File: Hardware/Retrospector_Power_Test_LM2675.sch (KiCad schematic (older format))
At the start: 21 parts, among them J2 Eurorack_10_pin_power, U1 TPS5410D, U2 LD1117-3.3-4Tab

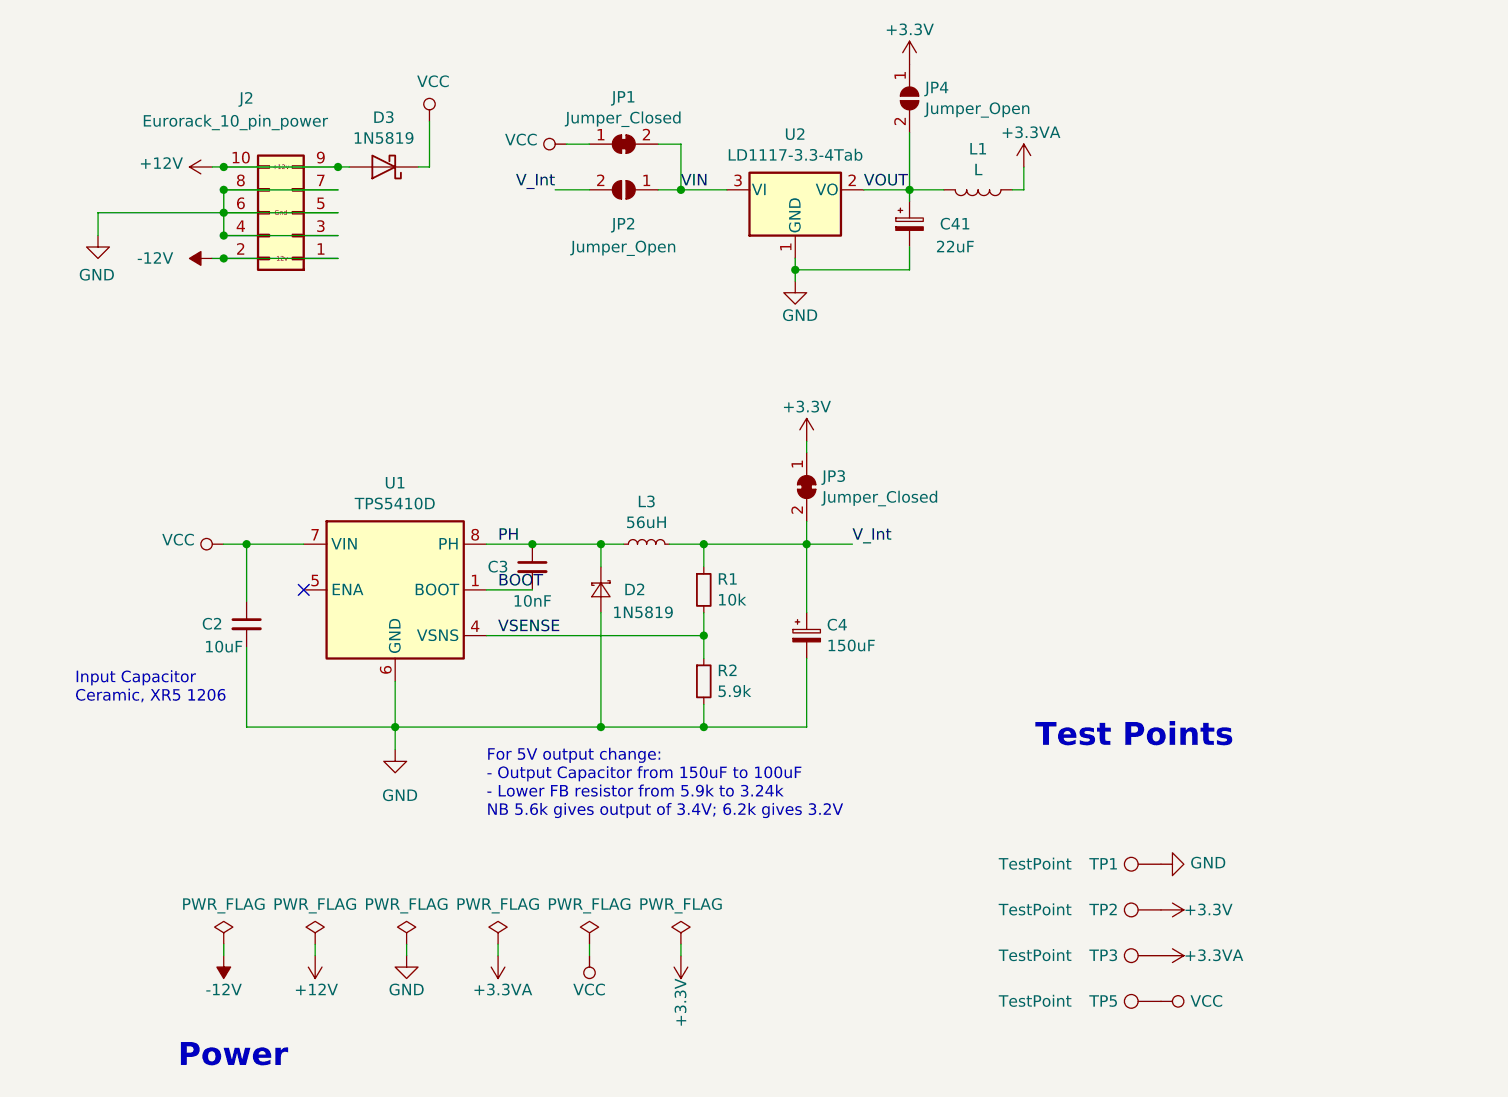
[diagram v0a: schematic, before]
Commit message: Initial schematics for power test boards with various chips
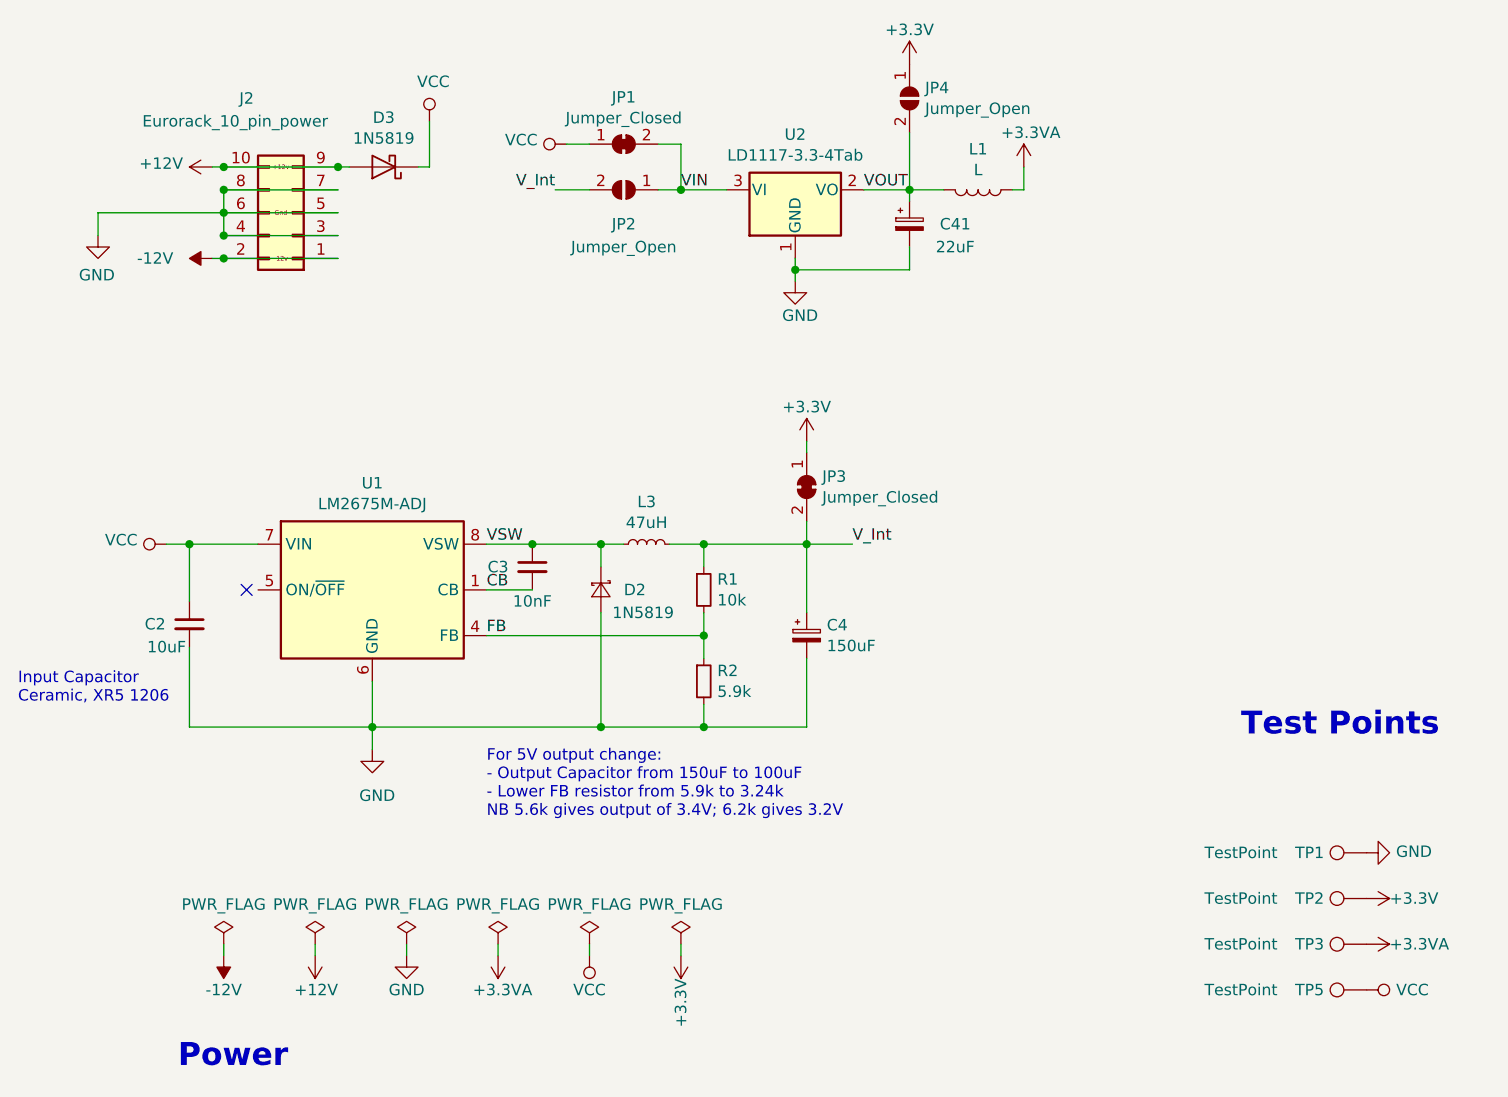
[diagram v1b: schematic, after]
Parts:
- removed U1: TPS5410D, Housings_SOIC:SOIC-8_3.9x4.9mm_Pitch1.27mm, symbol TPS5410DR:TPS5410D
- added U1: LM2675M-ADJ, Housings_SOIC:SOIC-8_3.9x4.9mm_Pitch1.27mm, symbol LM2675M-ADJ:LM2675M-ADJ
- L3: value 56uH -> 47uH; footprint Custom_Footprints:Inductor_SMD_6x6mm -> Inductors_SMD:L_6.3x6.3_H3
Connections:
- net GND: now also U1.6 (GND)
- net VCC: now also U1.7 (VIN)
- net BOOT renamed CB
- net CB: now also U1.1 (CB)
- net PH renamed VSW
- net VSW: now also U1.8 (VSW)
- net VSENSE renamed FB
- net FB: now also U1.4 (FB)
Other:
- moved on the sheet: C2, TP1, TP2, TP3, TP5
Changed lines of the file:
@@
 L Connector:TestPoint TP5
 U 1 1 5FBC912F
-P 5550 4950
-F 0 "TP5" V 5550 5200 50  0000 C CNN
-F 1 "TestPoint" V 5550 5500 50  0000 C CNN
-F 2 "Custom_Footprints:1.3mm_Test_Point" H 5750 4950 50  0001 C CNN
-F 3 "~" H 5750 4950 50  0001 C CNN
-	1    5550 4950
+P 6450 4900
+F 0 "TP5" V 6450 5150 50  0000 C CNN
+F 1 "TestPoint" V 6450 5450 50  0000 C CNN
+F 2 "Custom_Footprints:1.3mm_Test_Point" H 6650 4900 50  0001 C CNN
+F 3 "~" H 6650 4900 50  0001 C CNN
+	1    6450 4900
 	0    -1   -1   0
 $EndComp
@@
 L power:VCC #PWR018
 U 1 1 5FBC9909
-P 5550 4950
-F 0 "#PWR018" H 5550 4800 50  0001 C CNN
-F 1 "VCC" V 5550 5150 50  0000 C CNN
-F 2 "" H 5550 4950 50  0001 C CNN
-F 3 "" H 5550 4950 50  0001 C CNN
-	1    5550 4950
-	0    1    1    0
-$EndComp
-Text Notes 5000 3850 0    100  ~ 20
+P 6450 4900
+F 0 "#PWR018" H 6450 4750 50  0001 C CNN
+F 1 "VCC" V 6450 5100 50  0000 C CNN
+F 2 "" H 6450 4900 50  0001 C CNN
+F 3 "" H 6450 4900 50  0001 C CNN
+	1    6450 4900
+	0    1    1    0
+$EndComp
+Text Notes 5900 3800 0    100  ~ 20
 Test Points
 Wire Wire Line
@@
 L power:+3.3VA #PWR013
 U 1 1 5FBC8BDD
-P 5550 4750
-F 0 "#PWR013" H 5550 4600 50  0001 C CNN
-F 1 "+3.3VA" V 5550 4850 50  0000 L CNN
-F 2 "" H 5550 4750 50  0001 C CNN
-F 3 "" H 5550 4750 50  0001 C CNN
-	1    5550 4750
+P 6450 4700
+F 0 "#PWR013" H 6450 4550 50  0001 C CNN
+F 1 "+3.3VA" V 6450 4800 50  0000 L CNN
+F 2 "" H 6450 4700 50  0001 C CNN
+F 3 "" H 6450 4700 50  0001 C CNN
+	1    6450 4700
 	0    1    1    0
 $EndComp
@@
 L Connector:TestPoint TP3
 U 1 1 5FBC8AAF
-P 5550 4750
-F 0 "TP3" V 5550 5000 50  0000 C CNN
-F 1 "TestPoint" V 5550 5300 50  0000 C CNN
-F 2 "Custom_Footprints:1.3mm_Test_Point" H 5750 4750 50  0001 C CNN
-F 3 "~" H 5750 4750 50  0001 C CNN
-	1    5550 4750
+P 6450 4700
+F 0 "TP3" V 6450 4950 50  0000 C CNN
+F 1 "TestPoint" V 6450 5250 50  0000 C CNN
+F 2 "Custom_Footprints:1.3mm_Test_Point" H 6650 4700 50  0001 C CNN
+F 3 "~" H 6650 4700 50  0001 C CNN
+	1    6450 4700
 	0    -1   -1   0
 $EndComp
@@
 L power:+3.3V #PWR011
 U 1 1 5FBC8425
-P 5550 4550
-F 0 "#PWR011" H 5550 4400 50  0001 C CNN
-F 1 "+3.3V" V 5550 4650 50  0000 L CNN
-F 2 "" H 5550 4550 50  0001 C CNN
-F 3 "" H 5550 4550 50  0001 C CNN
-	1    5550 4550
+P 6450 4500
+F 0 "#PWR011" H 6450 4350 50  0001 C CNN
+F 1 "+3.3V" V 6450 4600 50  0000 L CNN
+F 2 "" H 6450 4500 50  0001 C CNN
+F 3 "" H 6450 4500 50  0001 C CNN
+	1    6450 4500
 	0    1    1    0
 $EndComp
@@
 L Connector:TestPoint TP2
 U 1 1 5FBC80EE
-P 5550 4550
-F 0 "TP2" V 5550 4800 50  0000 C CNN
-F 1 "TestPoint" V 5550 5100 50  0000 C CNN
-F 2 "Custom_Footprints:1.3mm_Test_Point" H 5750 4550 50  0001 C CNN
-F 3 "~" H 5750 4550 50  0001 C CNN
-	1    5550 4550
+P 6450 4500
+F 0 "TP2" V 6450 4750 50  0000 C CNN
+F 1 "TestPoint" V 6450 5050 50  0000 C CNN
+F 2 "Custom_Footprints:1.3mm_Test_Point" H 6650 4500 50  0001 C CNN
+F 3 "~" H 6650 4500 50  0001 C CNN
+	1    6450 4500
 	0    -1   -1   0
 $EndComp
@@
 L power:GND #PWR010
 U 1 1 5FBC7DF8
-P 5550 4350
-F 0 "#PWR010" H 5550 4100 50  0001 C CNN
-F 1 "GND" V 5555 4222 50  0000 R CNN
-F 2 "" H 5550 4350 50  0001 C CNN
-F 3 "" H 5550 4350 50  0001 C CNN
-	1    5550 4350
+P 6450 4300
+F 0 "#PWR010" H 6450 4050 50  0001 C CNN
+F 1 "GND" V 6455 4172 50  0000 R CNN
+F 2 "" H 6450 4300 50  0001 C CNN
+F 3 "" H 6450 4300 50  0001 C CNN
+	1    6450 4300
 	0    -1   -1   0
 $EndComp
@@
 L Connector:TestPoint TP1
 U 1 1 5FBC76F3
-P 5550 4350
-F 0 "TP1" V 5550 4600 50  0000 C CNN
-F 1 "TestPoint" V 5550 4900 50  0000 C CNN
-F 2 "Custom_Footprints:1.3mm_Test_Point" H 5750 4350 50  0001 C CNN
-F 3 "~" H 5750 4350 50  0001 C CNN
-	1    5550 4350
+P 6450 4300
+F 0 "TP1" V 6450 4550 50  0000 C CNN
+F 1 "TestPoint" V 6450 4850 50  0000 C CNN
+F 2 "Custom_Footprints:1.3mm_Test_Point" H 6650 4300 50  0001 C CNN
+F 3 "~" H 6650 4300 50  0001 C CNN
+	1    6450 4300
 	0    -1   -1   0
 $EndComp
 Wire Wire Line
 	1450 1500 900  1500
-$Comp
-L TPS5410DR:TPS5410D U1
-U 1 1 63B9AA59
-P 2200 3150
-F 0 "U1" H 2200 3617 50  0000 C CNN
-F 1 "TPS5410D" H 2200 3526 50  0000 C CNN
-F 2 "Housings_SOIC:SOIC-8_3.9x4.9mm_Pitch1.27mm" H 2150 3600 50  0001 C CNN
-F 3 "https://www.ti.com/lit/gpn/tps5410" H 2200 3150 50  0001 C CNN
-	1    2200 3150
-	1    0    0    -1
-$EndComp
 $Comp
 L Device:C_Small C3
@@
 Wire Wire Line
 	2600 3150 2800 3150
-NoConn ~ 1800 3150
+NoConn ~ 1550 3150
 $Comp
 L power:GND #PWR03
 U 1 1 63BB87EE
-P 2200 3850
-F 0 "#PWR03" H 2200 3600 50  0001 C CNN
-F 1 "GND" H 2300 3650 50  0000 R CNN
-F 2 "" H 2200 3850 50  0001 C CNN
-F 3 "" H 2200 3850 50  0001 C CNN
-	1    2200 3850
-	1    0    0    -1
-$EndComp
-Wire Wire Line
-	2200 3550 2200 3750
-Wire Wire Line
-	1800 2950 1550 2950
-Wire Wire Line
-	1550 2950 1550 3200
-Wire Wire Line
-	1550 3400 1550 3750
-Wire Wire Line
-	1550 3750 2200 3750
-Connection ~ 2200 3750
+P 2100 3850
+F 0 "#PWR03" H 2100 3600 50  0001 C CNN
+F 1 "GND" H 2200 3650 50  0000 R CNN
+F 2 "" H 2100 3850 50  0001 C CNN
+F 3 "" H 2100 3850 50  0001 C CNN
+	1    2100 3850
+	1    0    0    -1
+$EndComp
+Wire Wire Line
+	2100 3550 2100 3750
+Wire Wire Line
+	1600 2950 1300 2950
+Wire Wire Line
+	1300 2950 1300 3200
+Wire Wire Line
+	1300 3400 1300 3750
+Wire Wire Line
+	1300 3750 2100 3750
+Connection ~ 2100 3750
 $Comp
 L power:VCC #PWR01
 U 1 1 63BCE4C9
-P 1450 2950
-F 0 "#PWR01" H 1450 2800 50  0001 C CNN
-F 1 "VCC" V 1468 3077 50  0000 L CNN
-F 2 "" H 1450 2950 50  0001 C CNN
-F 3 "" H 1450 2950 50  0001 C CNN
-	1    1450 2950
-	0    -1   -1   0
-$EndComp
-Wire Wire Line
-	1450 2950 1550 2950
-Connection ~ 1550 2950
-Wire Wire Line
-	2200 3850 2200 3750
+P 1200 2950
+F 0 "#PWR01" H 1200 2800 50  0001 C CNN
+F 1 "VCC" V 1218 3077 50  0000 L CNN
+F 2 "" H 1200 2950 50  0001 C CNN
+F 3 "" H 1200 2950 50  0001 C CNN
+	1    1200 2950
+	0    -1   -1   0
+$EndComp
+Wire Wire Line
+	1200 2950 1300 2950
+Connection ~ 1300 2950
+Wire Wire Line
+	2100 3850 2100 3750
 Connection ~ 3550 3750
 Wire Wire Line
@@
 P 3300 2950
 F 0 "L3" V 3485 2950 50  0000 C CNN
-F 1 "56uH" V 3394 2950 50  0000 C CNN
-F 2 "Custom_Footprints:Inductor_SMD_6x6mm" H 3300 2950 50  0001 C CNN
-F 3 "https://datasheet.lcsc.com/szlcsc/1912111437_3L-COILS-SNR6045K-680M_C326343.pdf" H 3300 2950 50  0001 C CNN
+F 1 "47uH" V 3394 2950 50  0000 C CNN
+F 2 "Inductors_SMD:L_6.3x6.3_H3" H 3300 2950 50  0001 C CNN
+F 3 "https://www.mouser.com/datasheet/2/400/nductor_automotive_power_clf7045-d_en-1280129.pdf" H 3300 2950 50  0001 C CNN
 F 4 "C326343" V 3300 2950 50  0001 C CNN "Part_Number"
 	1    3300 2950
@@
 	3100 3250 3100 3750
 Wire Wire Line
-	3100 3750 2200 3750
-Connection ~ 3100 3750
+	3100 3750 2100 3750
 $Comp
 L power:+3.3V #PWR04
@@
 Text Notes 2600 4150 0    50   ~ 0
 For 5V output change:\n- Output Capacitor from 150uF to 100uF\n- Lower FB resistor from 5.9k to 3.24k\nNB 5.6k gives output of 3.4V; 6.2k gives 3.2V
-Text Notes 800  3650 0    50   ~ 0
+Text Notes 550  3650 0    50   ~ 0
 Input Capacitor\nCeramic, XR5 1206
 $Comp
 L Device:C_Small C2
 U 1 1 63C237DB
-P 1550 3300
-F 0 "C2" H 1400 3300 50  0000 C CNN
-F 1 "10uF" H 1450 3200 50  0000 C CNN
-F 2 "Capacitors_SMD:C_1206" H 1550 3300 50  0001 C CNN
-F 3 "~" H 1550 3300 50  0001 C CNN
-F 4 "C57112" H 1550 3300 50  0001 C CNN "Part_Number"
-	1    1550 3300
+P 1300 3300
+F 0 "C2" H 1150 3300 50  0000 C CNN
+F 1 "10uF" H 1200 3200 50  0000 C CNN
+F 2 "Capacitors_SMD:C_1206" H 1300 3300 50  0001 C CNN
+F 3 "~" H 1300 3300 50  0001 C CNN
+F 4 "C57112" H 1300 3300 50  0001 C CNN "Part_Number"
+	1    1300 3300
 	1    0    0    -1
 $EndComp
@@
 Wire Wire Line
 	4250 1400 4450 1400
-Text Label 2650 3350 0    50   ~ 0
-VSENSE
-Text Label 2650 2950 0    50   ~ 0
-PH
-Text Label 2650 3150 0    50   ~ 0
-BOOT
+Text Label 2600 3350 0    50   ~ 0
+FB
+Text Label 2600 2950 0    50   ~ 0
+VSW
+Text Label 2600 3150 0    50   ~ 0
+CB
 Text Label 4250 1400 0    50   ~ 0
 VOUT
@@
 	-1   0    0    1
 $EndComp
+Connection ~ 3100 3750
+$Comp
+L LM2675M-ADJ:LM2675M-ADJ U1
+U 1 1 5FBEEB41
+P 2100 3150
+F 0 "U1" H 2100 3617 50  0000 C CNN
+F 1 "LM2675M-ADJ" H 2100 3526 50  0000 C CNN
+F 2 "Housings_SOIC:SOIC-8_3.9x4.9mm_Pitch1.27mm" H 2150 2800 50  0001 L CIN
+F 3 "https://www.ti.com/lit/gpn/lm2675" H 2100 3150 50  0001 C CNN
+	1    2100 3150
+	1    0    0    -1
+$EndComp
 $EndSCHEMATC
